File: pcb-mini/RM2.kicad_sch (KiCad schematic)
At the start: 3 parts, among them J8 Conn_01x21_Pin

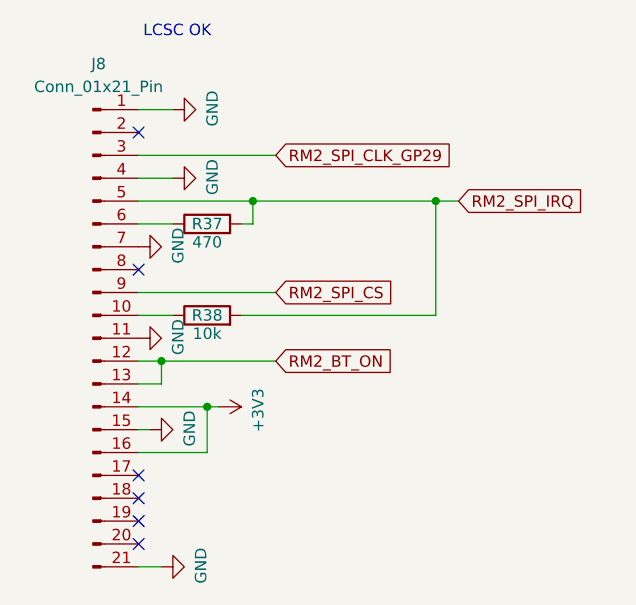
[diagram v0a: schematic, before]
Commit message: [pcb] mini: add/fix LCSC refs
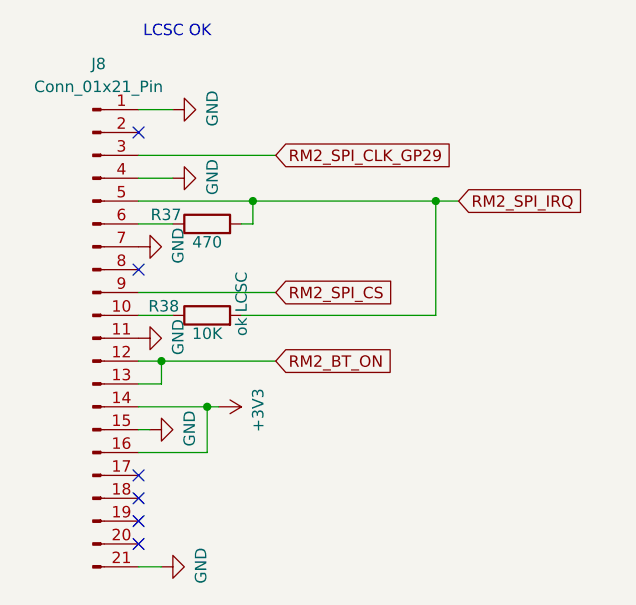
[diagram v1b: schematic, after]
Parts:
- R38: value 10k -> 10K; footprint Resistor_SMD:R_0603_1608Metric -> Resistor_SMD:R_0402_1005Metric; LCSC C25804 -> C25744
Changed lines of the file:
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@@
 		(dnp no)
 		(property "Reference" "R38"
-			(at 132.08 91.44 90)
-			(effects
-				(font
-					(size 1.27 1.27)
-				)
-			)
-		)
-		(property "Value" "10k"
+			(at 127.254 90.424 90)
+			(effects
+				(font
+					(size 1.27 1.27)
+				)
+			)
+		)
+		(property "Value" "10K"
 			(at 132.08 93.472 90)
 			(effects
@@
 			)
 		)
-		(property "Footprint" "Resistor_SMD:R_0603_1608Metric"
+		(property "Footprint" "Resistor_SMD:R_0402_1005Metric"
 			(at 132.08 93.218 90)
 			(effects
@@
 			)
 		)
-		(property "Description" ""
-			(at 132.08 91.44 0)
-			(effects
-				(font
-					(size 1.27 1.27)
-				)
-				(hide yes)
-			)
-		)
-		(property "LCSC" "C25804"
+		(property "Description" "ok LCSC"
+			(at 135.89 90.17 0)
+			(effects
+				(font
+					(size 1.27 1.27)
+				)
+			)
+		)
+		(property "LCSC" "C25744"
 			(at 132.08 91.44 90)
 			(effects
@@
 		(dnp no)
 		(property "Reference" "R37"
-			(at 132.08 81.28 90)
-			(effects
-				(font
+			(at 127.508 80.264 90)
+			(effects
+				(font
